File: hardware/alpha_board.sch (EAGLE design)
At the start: 22 parts, among them Y1 32.768kHz

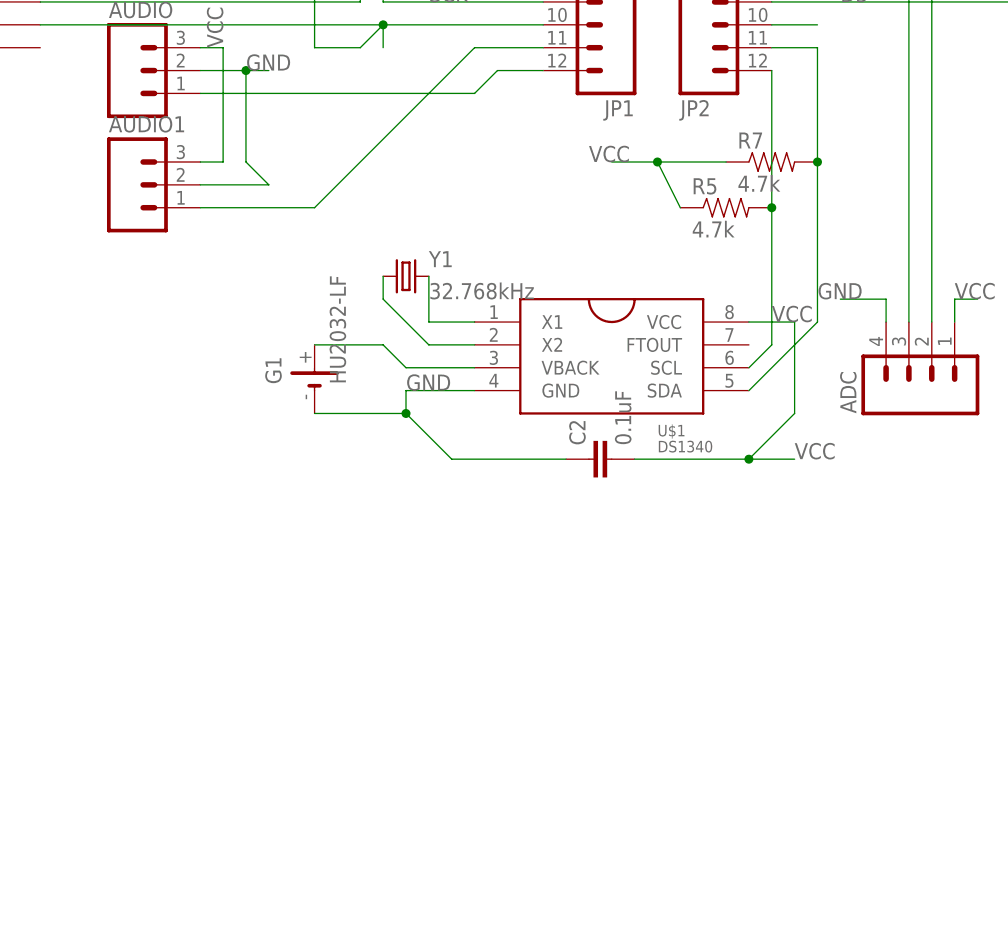
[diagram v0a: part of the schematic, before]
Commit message: hardware update, new RTC chip, smaller footprint
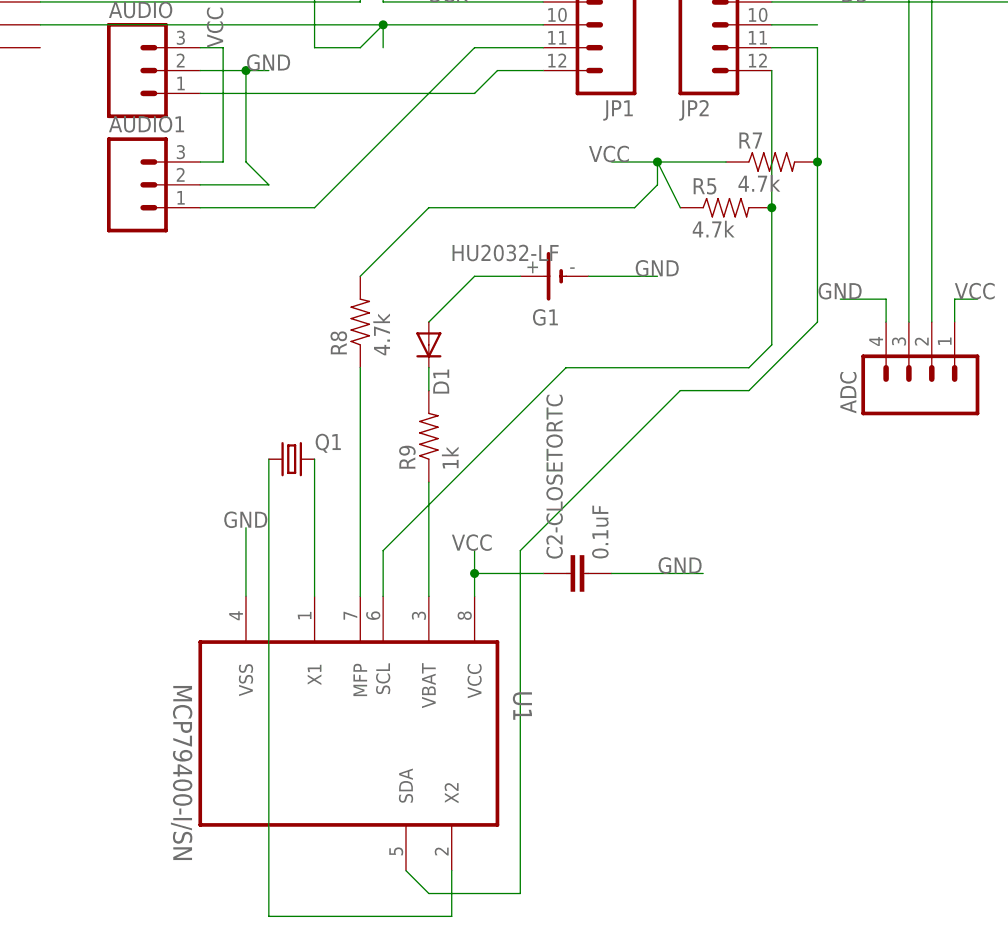
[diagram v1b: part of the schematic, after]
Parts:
- removed C2: 0.1uF, SparkFun-Capacitors:0.1UF-25V(+80/-20%)(0603)
- removed U$1: DS1340, carrilib:DS1340
- removed Y1: 32.768kHz, SparkFun-FreqCtrl:CRYSTALTC26H
- added C2-CLOSETORTC: 0.1uF, SparkFun-Capacitors:0.1UF-25V(+80/-20%)(0603)
- added D1: (no value), diode:DIODE-SOD323-W
- added Q1: (no value), Hangar:CRYSTALABS10
- added R8: 4.7k, SparkFun:RESISTOR1206
- added R9: 1k, SparkFun:RESISTOR1206
- added U1: MCP79400-I/SN, Microchip-MCP79400-I_SN:MCP79400-I/SN
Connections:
- new net N$10: D1.A, G1.+
- new net N$12: R9.1, U1.VBAT
- new net N$8: R8.1, U1.MFP
- net GND: now also C2-CLOSETORTC.2, U1.VSS; no longer C2.1, U$1.GND
- net N$11: now also U1.SDA; no longer U$1.SDA
- net N$3: now also Q1.1, U1.X2; no longer U$1.X1, Y1.2
- net N$4: now also Q1.2, U1.X1; no longer G1.+, U$1.VBACK
- net N$5: now also D1.C, R9.2; no longer U$1.X2, Y1.1
- net N$9: now also U1.SCL; no longer U$1.SCL
- net VCC: now also C2-CLOSETORTC.1, R8.2, U1.VCC; no longer C2.2, U$1.VCC
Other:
- moved on the sheet: G1
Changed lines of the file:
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@@
 <part name="R4" library="SparkFun" deviceset="RESISTOR" device="1206"/>
 <part name="AUDIO1" library="SparkFun" deviceset="M03" device="LOCK"/>
-<part name="U$1" library="carrilib" deviceset="DS1340" device=""/>
 <part name="G1" library="Simplex-Battery" deviceset="HU2032-LF" device=""/>
-<part name="Y1" library="SparkFun-FreqCtrl" deviceset="CRYSTAL" device="TC26H" value="32.768kHz"/>
 <part name="R5" library="SparkFun" deviceset="RESISTOR" device="1206" value="4.7k"/>
 <part name="R7" library="SparkFun" deviceset="RESISTOR" device="1206" value="4.7k"/>
-<part name="C2" library="SparkFun-Capacitors" deviceset="0.1UF-25V(+80/-20%)(0603)" device="" value="0.1uF"/>
+<part name="C2-CLOSETORTC" library="SparkFun-Capacitors" deviceset="0.1UF-25V(+80/-20%)(0603)" device="" value="0.1uF"/>
+<part name="U1" library="Microchip-MCP79400-I_SN" deviceset="MCP79400-I/SN" device=""/>
+<part name="R8" library="SparkFun" deviceset="RESISTOR" device="1206" value="4.7k"/>
+<part name="D1" library="diode" deviceset="DIODE-" device="SOD323-W"/>
+<part name="R9" library="SparkFun" deviceset="RESISTOR" device="1206" value="1k"/>
+<part name="Q1" library="Hangar" deviceset="CRYSTAL" device="ABS10"/>
 </parts>
 <sheets>
@@
 <instance part="R4" gate="G$1" x="-10.16" y="35.56" rot="R90"/>
 <instance part="AUDIO1" gate="G$1" x="-30.48" y="-10.16"/>
-<instance part="U$1" gate="G$1" x="22.86" y="-30.48"/>
-<instance part="G1" gate="BAT" x="-10.16" y="-30.48" rot="R90"/>
-<instance part="Y1" gate="G$1" x="0" y="-20.32"/>
+<instance part="G1" gate="BAT" x="15.24" y="-20.32" rot="R180"/>
 <instance part="R5" gate="G$1" x="35.56" y="-12.7"/>
 <instance part="R7" gate="G$1" x="40.64" y="-7.62"/>
-<instance part="C2" gate="G$1" x="22.86" y="-40.64" rot="R90"/>
+<instance part="C2-CLOSETORTC" gate="G$1" x="20.32" y="-53.34" rot="R90"/>
+<instance part="U1" gate="A" x="-2.54" y="-71.12" rot="R270"/>
+<instance part="R8" gate="G$1" x="-5.08" y="-25.4" rot="R90"/>
+<instance part="D1" gate="G$1" x="2.54" y="-27.94" rot="R270"/>
+<instance part="R9" gate="G$1" x="2.54" y="-38.1" rot="R90"/>
+<instance part="Q1" gate="G$1" x="-12.7" y="-40.64"/>
 </instances>
 <busses>
@@
 </segment>
 <segment>
-<pinref part="U$1" gate="G$1" pin="GND"/>
-<wire x1="7.62" y1="-33.02" x2="0" y2="-33.02" width="0.1524" layer="91"/>
-<label x="0" y="-33.02" size="1.778" layer="95"/>
+<pinref part="U1" gate="A" pin="VSS"/>
+<wire x1="-17.78" y1="-55.88" x2="-17.78" y2="-48.26" width="0.1524" layer="91"/>
+<label x="-20.32" y="-48.26" size="1.778" layer="95"/>
+</segment>
+<segment>
+<pinref part="C2-CLOSETORTC" gate="G$1" pin="2"/>
+<wire x1="22.86" y1="-53.34" x2="33.02" y2="-53.34" width="0.1524" layer="91"/>
+<label x="27.94" y="-53.34" size="1.778" layer="95"/>
+</segment>
+<segment>
 <pinref part="G1" gate="BAT" pin="-"/>
-<wire x1="-10.16" y1="-35.56" x2="0" y2="-35.56" width="0.1524" layer="91"/>
-<wire x1="0" y1="-35.56" x2="0" y2="-33.02" width="0.1524" layer="91"/>
-<wire x1="0" y1="-35.56" x2="5.08" y2="-40.64" width="0.1524" layer="91"/>
-<junction x="0" y="-35.56"/>
-<pinref part="C2" gate="G$1" pin="1"/>
-<wire x1="5.08" y1="-40.64" x2="17.78" y2="-40.64" width="0.1524" layer="91"/>
+<wire x1="20.32" y1="-20.32" x2="27.94" y2="-20.32" width="0.1524" layer="91"/>
+<label x="25.4" y="-20.32" size="1.778" layer="95"/>
 </segment>
 </net>
@@
 </segment>
 <segment>
-<pinref part="U$1" gate="G$1" pin="VCC"/>
-<wire x1="38.1" y1="-25.4" x2="43.18" y2="-25.4" width="0.1524" layer="91"/>
-<label x="40.64" y="-25.4" size="1.778" layer="95"/>
-<pinref part="C2" gate="G$1" pin="2"/>
-<wire x1="25.4" y1="-40.64" x2="38.1" y2="-40.64" width="0.1524" layer="91"/>
-<wire x1="38.1" y1="-40.64" x2="43.18" y2="-35.56" width="0.1524" layer="91"/>
-<wire x1="43.18" y1="-35.56" x2="43.18" y2="-25.4" width="0.1524" layer="91"/>
-<wire x1="38.1" y1="-40.64" x2="43.18" y2="-40.64" width="0.1524" layer="91"/>
-<junction x="38.1" y="-40.64"/>
-<label x="43.18" y="-40.64" size="1.778" layer="95"/>
-</segment>
-<segment>
 <pinref part="R7" gate="G$1" pin="1"/>
 <wire x1="35.56" y1="-7.62" x2="27.94" y2="-7.62" width="0.1524" layer="91"/>
@@
 <junction x="27.94" y="-7.62"/>
 <label x="20.32" y="-7.62" size="1.778" layer="95"/>
+<pinref part="R8" gate="G$1" pin="2"/>
+<wire x1="-5.08" y1="-20.32" x2="2.54" y2="-12.7" width="0.1524" layer="91"/>
+<wire x1="2.54" y1="-12.7" x2="25.4" y2="-12.7" width="0.1524" layer="91"/>
+<wire x1="25.4" y1="-12.7" x2="27.94" y2="-10.16" width="0.1524" layer="91"/>
+<wire x1="27.94" y1="-10.16" x2="27.94" y2="-7.62" width="0.1524" layer="91"/>
 </segment>
 <segment>
@@
 <wire x1="-22.86" y1="-7.62" x2="-20.32" y2="-7.62" width="0.1524" layer="91"/>
 <wire x1="-20.32" y1="-7.62" x2="-20.32" y2="5.08" width="0.1524" layer="91"/>
+</segment>
+<segment>
+<pinref part="U1" gate="A" pin="VCC"/>
+<wire x1="7.62" y1="-55.88" x2="7.62" y2="-53.34" width="0.1524" layer="91"/>
+<pinref part="C2-CLOSETORTC" gate="G$1" pin="1"/>
+<wire x1="7.62" y1="-53.34" x2="7.62" y2="-50.8" width="0.1524" layer="91"/>
+<wire x1="15.24" y1="-53.34" x2="7.62" y2="-53.34" width="0.1524" layer="91"/>
+<junction x="7.62" y="-53.34"/>
+<label x="5.08" y="-50.8" size="1.778" layer="95"/>
 </segment>
 </net>
@@
 </segment>
 </net>
-<net name="N$4" class="0">
-<segment>
-<pinref part="G1" gate="BAT" pin="+"/>
-<wire x1="-10.16" y1="-27.94" x2="-2.54" y2="-27.94" width="0.1524" layer="91"/>
-<wire x1="-2.54" y1="-27.94" x2="0" y2="-30.48" width="0.1524" layer="91"/>
-<pinref part="U$1" gate="G$1" pin="VBACK"/>
-<wire x1="7.62" y1="-30.48" x2="0" y2="-30.48" width="0.1524" layer="91"/>
-</segment>
-</net>
-<net name="N$3" class="0">
-<segment>
-<pinref part="Y1" gate="G$1" pin="2"/>
-<wire x1="2.54" y1="-20.32" x2="2.54" y2="-25.4" width="0.1524" layer="91"/>
-<pinref part="U$1" gate="G$1" pin="X1"/>
-<wire x1="2.54" y1="-25.4" x2="7.62" y2="-25.4" width="0.1524" layer="91"/>
-</segment>
-</net>
-<net name="N$5" class="0">
-<segment>
-<pinref part="U$1" gate="G$1" pin="X2"/>
-<wire x1="7.62" y1="-27.94" x2="2.54" y2="-27.94" width="0.1524" layer="91"/>
-<wire x1="2.54" y1="-27.94" x2="-2.54" y2="-22.86" width="0.1524" layer="91"/>
-<pinref part="Y1" gate="G$1" pin="1"/>
-<wire x1="-2.54" y1="-22.86" x2="-2.54" y2="-20.32" width="0.1524" layer="91"/>
-</segment>
-</net>
 <net name="N$9" class="0">
 <segment>
-<pinref part="U$1" gate="G$1" pin="SCL"/>
 <wire x1="38.1" y1="-30.48" x2="40.64" y2="-27.94" width="0.1524" layer="91"/>
 <pinref part="R5" gate="G$1" pin="2"/>
@@
 <wire x1="40.64" y1="-12.7" x2="40.64" y2="2.54" width="0.1524" layer="91"/>
 <junction x="40.64" y="-12.7"/>
+<pinref part="U1" gate="A" pin="SCL"/>
+<wire x1="-2.54" y1="-55.88" x2="-2.54" y2="-50.8" width="0.1524" layer="91"/>
+<wire x1="-2.54" y1="-50.8" x2="17.78" y2="-30.48" width="0.1524" layer="91"/>
+<wire x1="17.78" y1="-30.48" x2="38.1" y2="-30.48" width="0.1524" layer="91"/>
 </segment>
 </net>
@@
 <segment>
 <pinref part="R7" gate="G$1" pin="2"/>
-<pinref part="U$1" gate="G$1" pin="SDA"/>
 <wire x1="45.72" y1="-7.62" x2="45.72" y2="-25.4" width="0.1524" layer="91"/>
 <wire x1="45.72" y1="-25.4" x2="38.1" y2="-33.02" width="0.1524" layer="91"/>
@@
 <pinref part="JP2" gate="G$1" pin="11"/>
 <wire x1="45.72" y1="5.08" x2="40.64" y2="5.08" width="0.1524" layer="91"/>
-</segment>
-</net>
+<pinref part="U1" gate="A" pin="SDA"/>
+<wire x1="0" y1="-86.36" x2="2.54" y2="-88.9" width="0.1524" layer="91"/>
+<wire x1="2.54" y1="-88.9" x2="12.7" y2="-88.9" width="0.1524" layer="91"/>
+<wire x1="12.7" y1="-88.9" x2="12.7" y2="-50.8" width="0.1524" layer="91"/>
+<wire x1="12.7" y1="-50.8" x2="30.48" y2="-33.02" width="0.1524" layer="91"/>
+<wire x1="30.48" y1="-33.02" x2="38.1" y2="-33.02" width="0.1524" layer="91"/>
+</segment>
+</net>
+<net name="N$3" class="0">
+<segment>
+<pinref part="U1" gate="A" pin="X2"/>
+<wire x1="5.08" y1="-86.36" x2="5.08" y2="-91.44" width="0.1524" layer="91"/>
+<wire x1="5.08" y1="-91.44" x2="-15.24" y2="-91.44" width="0.1524" layer="91"/>
+<wire x1="-15.24" y1="-91.44" x2="-15.24" y2="-40.64" width="0.1524" layer="91"/>
+<pinref part="Q1" gate="G$1" pin="1"/>
+</segment>
+</net>
+<net name="N$4" class="0">
+<segment>
+<pinref part="U1" gate="A" pin="X1"/>
+<wire x1="-10.16" y1="-40.64" x2="-10.16" y2="-55.88" width="0.1524" layer="91"/>
+<pinref part="Q1" gate="G$1" pin="2"/>
+</segment>
+</net>
+<net name="N$8" class="0">
+<segment>
+<pinref part="U1" gate="A" pin="MFP"/>
+<wire x1="-5.08" y1="-55.88" x2="-5.08" y2="-30.48" width="0.1524" layer="91"/>
+<pinref part="R8" gate="G$1" pin="1"/>
+</segment>
+</net>
+<net name="N$5" class="0">
+<segment>
+<pinref part="R9" gate="G$1" pin="2"/>
+<pinref part="D1" gate="G$1" pin="C"/>
+<wire x1="2.54" y1="-33.02" x2="2.54" y2="-30.48" width="0.1524" layer="91"/>
+</segment>
+</net>
+<net name="N$10" class="0">
+<segment>
+<pinref part="D1" gate="G$1" pin="A"/>
+<pinref part="G1" gate="BAT" pin="+"/>
+<wire x1="2.54" y1="-25.4" x2="7.62" y2="-20.32" width="0.1524" layer="91"/>
+<wire x1="7.62" y1="-20.32" x2="12.7" y2="-20.32" width="0.1524" layer="91"/>
+</segment>
+</net>
+<net name="N$12" class="0">
+<segment>
+<pinref part="R9" gate="G$1" pin="1"/>
+<pinref part="U1" gate="A" pin="VBAT"/>
+<wire x1="2.54" y1="-43.18" x2="2.54" y2="-55.88" width="0.1524" layer="91"/>
+</segment>
+</net>

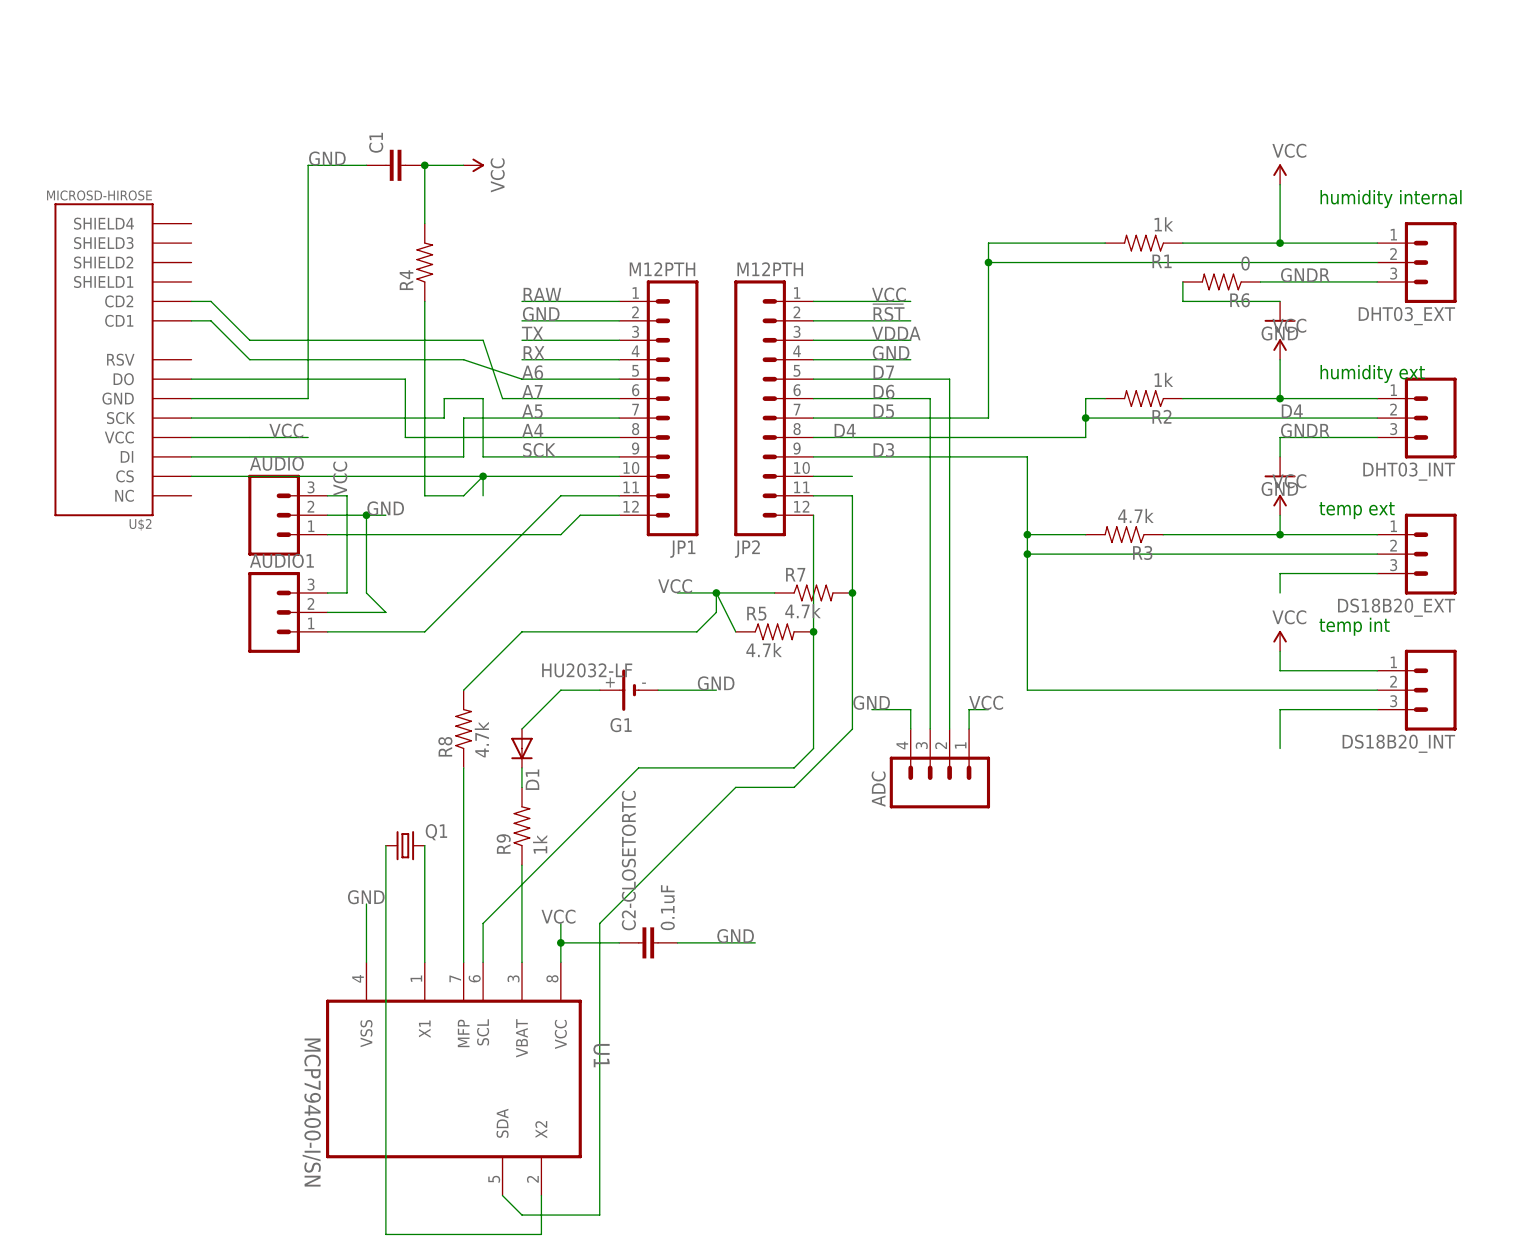
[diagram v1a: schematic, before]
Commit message: new PCB design without external RTC, thanks Angel M!
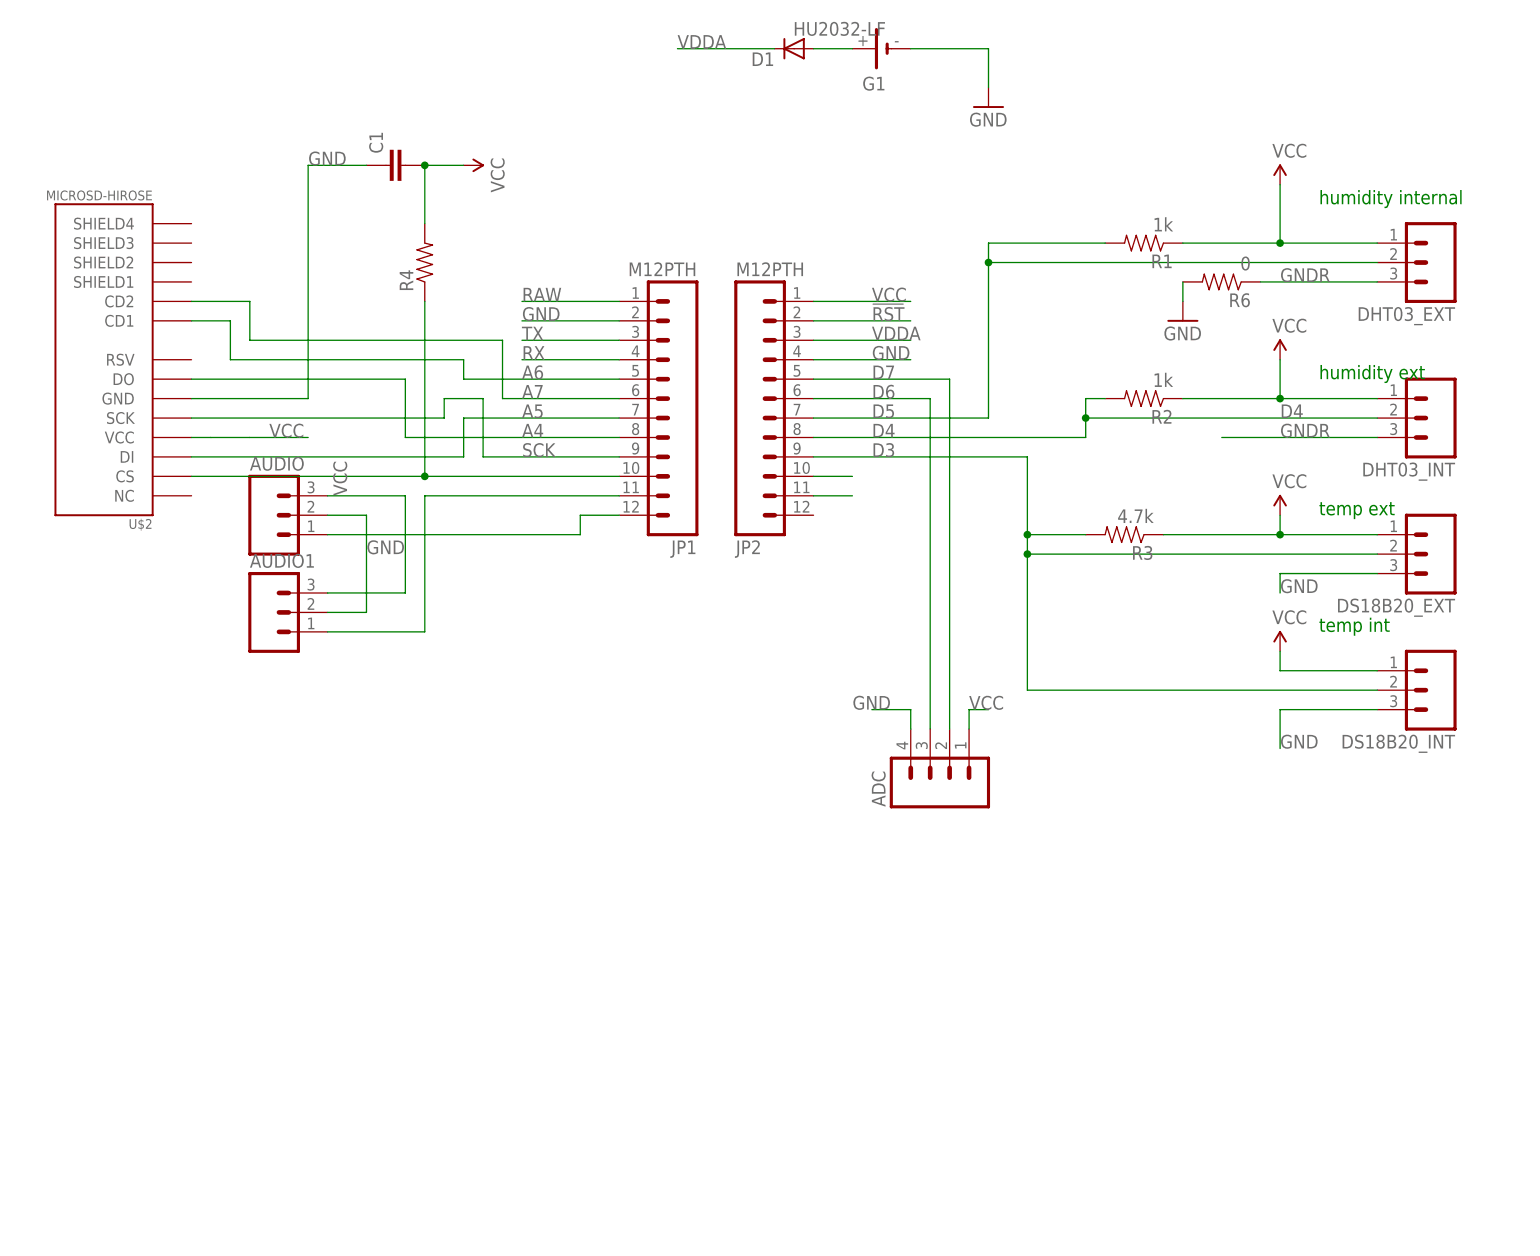
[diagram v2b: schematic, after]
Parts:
- removed C2-CLOSETORTC: 0.1uF, SparkFun-Capacitors:0.1UF-25V(+80/-20%)(0603)
- removed Q1: (no value), Hangar:CRYSTALABS10
- removed R5, R7, R8: 4.7k, SparkFun:RESISTOR1206
- removed R9: 1k, SparkFun:RESISTOR1206
- removed U1: MCP79400-I/SN, Microchip-MCP79400-I_SN:MCP79400-I/SN
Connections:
- removed net N$11: JP2.11, R7.2, U1.SDA
- removed net N$12: R9.1, U1.VBAT
- removed net N$3 (its old number): Q1.1, U1.X2
- removed net N$5: D1.C, R9.2
- removed net N$8: R8.1, U1.MFP
- removed net N$9: JP2.12, R5.2, U1.SCL
- net GND: no longer C2-CLOSETORTC.2, U1.VSS
- net N$4: now also JP2.11; no longer Q1.2, U1.X1
- net VCC: no longer C2-CLOSETORTC.1, R5.1, R7.1, R8.2, U1.VCC
- net VDDA: now also D1.C
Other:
- moved on the sheet: D1, G1
